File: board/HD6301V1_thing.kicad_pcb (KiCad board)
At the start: 2 copper layers, 99.1 x 86.4 mm, 53 parts, among them J1 KMDGX-6S-BS, J2 ps2_i2c, J3 P1_connector, J4 memmap_i2c, J5 8bit_thing_bus_connector, J6 USB_B_Micro, J7 prog_LED, J8 pwr_LED, SW1 Reset, SW2 Banking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

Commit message: HD6301 board: add GreenPAK i2c pullups
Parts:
- added R12: 10k, Resistor_SMD:R_0805_2012Metric_Pad1.20x1.40mm_HandSolder, F.Cu at (105.4, 57.0)
- added R13: 10k, Resistor_SMD:R_0805_2012Metric_Pad1.20x1.40mm_HandSolder, F.Cu at (105.4, 59.6)
- added R14: 10k, Resistor_SMD:R_0805_2012Metric_Pad1.20x1.40mm_HandSolder, F.Cu at (91.2, 99.1)
- added R15: 10k, Resistor_SMD:R_0805_2012Metric_Pad1.20x1.40mm_HandSolder, F.Cu at (91.2, 97.2)
- J2, J4: footprint Connector_PinHeader_2.54mm:PinHeader_1x02_P2.54mm_Vertical -> own_footprints:PinHeader_1x02_P2.54mm_Vertical_minimal
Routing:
- net Net-(J4-Pin_2): track 3.69 -> 7.41 mm, vias 0 -> 1
- net Net-(J4-Pin_1): track 7.12 -> 10.8 mm, vias 0 -> 1
- net Net-(J2-Pin_1): track 6.63 -> 8.98 mm
- net +5V: track 452.3 -> 454.3 mm
- net Net-(J2-Pin_2): track 5.09 -> 6.69 mm
- net /DATA_K: track 55.1 -> 56.6 mm
- net /CLK_K: track 51.2 -> 52.5 mm
- net /A12: track 91.8 -> 90.7 mm
- net /R/~{W}: track 99.7 -> 100.2 mm
- net /~{IRQ_K}: track 60.1 -> 60.3 mm, vias 0 -> 2

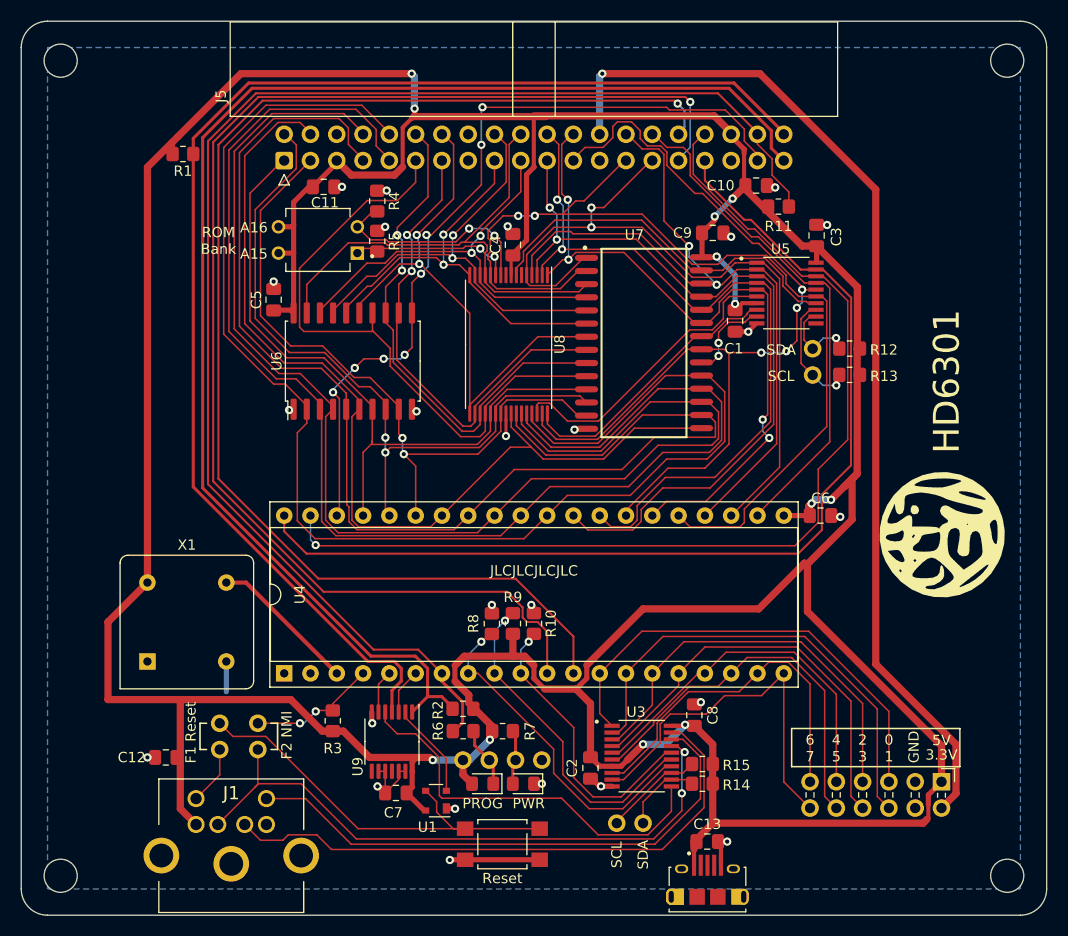
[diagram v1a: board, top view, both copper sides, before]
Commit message: HD6301 board: tie address latch OE to standby
This makes the address latch let go of the bus on standby which simplifies the
pico programmer.
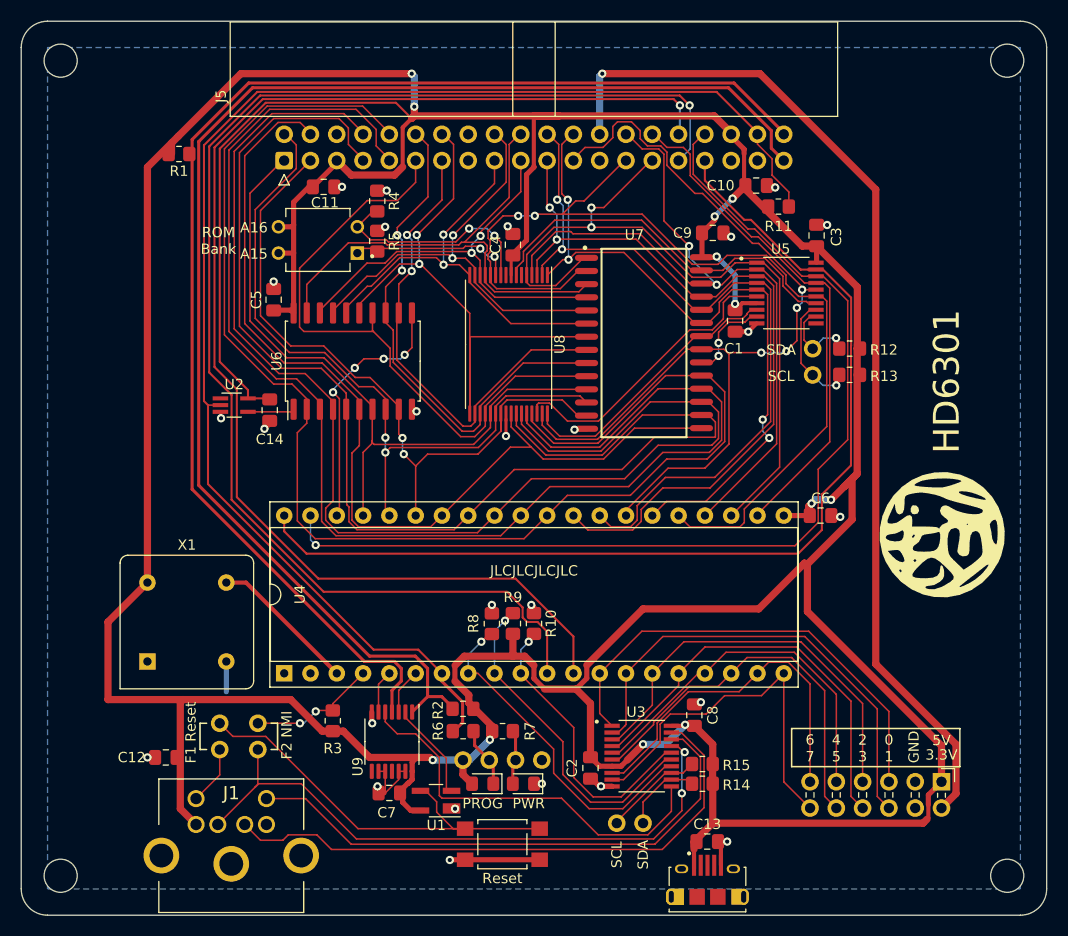
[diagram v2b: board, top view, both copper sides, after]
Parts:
- added C14: 100n, Capacitor_SMD:C_0805_2012Metric_Pad1.18x1.45mm_HandSolder, F.Cu at (49.4, 63.0)
- added U2: SN74LVC1G14DRL, Package_TO_SOT_SMD:SOT-353_SC-70-5_Handsoldering, F.Cu at (46.0, 62.5)
- U1: footprint Package_TO_SOT_SMD:SOT-143 -> Package_TO_SOT_SMD:SOT-143_Handsoldering
- moved C7 0.63 mm to (61.0, 99.9)
- moved R1 0.38 mm to (40.6, 38.2)
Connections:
- J5 pad 37: /AS -> unconnected-(J5-C1-Pad37)
- U6 pad 1: GND -> /LATCH_OE
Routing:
- net /AS: track 77.1 -> 24.8 mm, vias 8 -> 4
- net +5V: track 454.3 -> 504.4 mm
- net /LATCH_OE: track 0.00 -> 4.51 mm
- net /A3: track 53.6 -> 57.4 mm
- net /D2: track 65.2 -> 67.0 mm
- net /~{STBY}: track 134.9 -> 136.5 mm
- net /D7: track 132.8 -> 132.2 mm
- net GND: vias 25 -> 26

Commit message: Final version of HD6301V1 v1 board
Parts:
- added D3: BAT54W, Package_TO_SOT_SMD:SOT-323_SC-70_Handsoldering, F.Cu at (64.3, 93.5)
- moved U9 1.91 mm to (59.3, 95.0)
- moved R3 1.55 mm to (54.0, 92.7)
- moved C7 0.78 mm to (60.2, 99.9)
- moved R1 0.38 mm to (40.3, 38.2)
- moved R14 0.13 mm to (91.3, 99.1)
- moved R15 0.13 mm to (91.3, 97.2)
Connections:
- U3 pad 14: /P20 -> /CLK_K
- U3 pad 15: /P21 -> /DATA_K
- U3 pad 16: /P22 -> /~{IRQ_K}
- U3 pad 17: /~{IRQ_K} -> /P20
- U3 pad 18: /CLK_K -> /P21
- U3 pad 19: /DATA_K -> /P22
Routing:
- net Net-(D3-A): track 41.0 -> 48.0 mm
- net /~{STBY}: track 136.5 -> 140.5 mm
- net GND: track 44.2 -> 48.3 mm, vias 26 -> 28
- net Net-(U1-~{RESET}): track 8.72 -> 11.8 mm
- net Net-(U3-O6): track 38.6 -> 41.4 mm
- net /~{RESET_B}: track 133.1 -> 135.5 mm
- net /P21: track 31.8 -> 33.9 mm
- net /~{IRQ_B}: track 127.1 -> 129.2 mm
- net /P20: track 32.2 -> 34.1 mm
- net /P22: track 26.8 -> 28.7 mm
- net /~{IRQ_K}: track 60.3 -> 61.8 mm
- net Net-(U4-~{IRQ1}): track 4.17 -> 4.96 mm
- net /CLK_K: track 52.5 -> 53.2 mm

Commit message: HD6301 board: fix swapped SC1/SC2 pins
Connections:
- U4 pad 38: /AS -> /R/~{W}
- U4 pad 39: /R/~{W} -> /AS
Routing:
- net /D6: track 129.4 -> 132.4 mm
- net /R/~{W}: track 100.4 -> 97.7 mm
- net /D5: track 122.8 -> 124.4 mm
- net /AS: track 24.8 -> 25.9 mm
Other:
- board text added: "HD6301 V1.1"
- board text removed: "HD6301 V1.0"
